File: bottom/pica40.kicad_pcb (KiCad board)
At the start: 2 copper layers, 135 x 93.7 mm, 5 parts

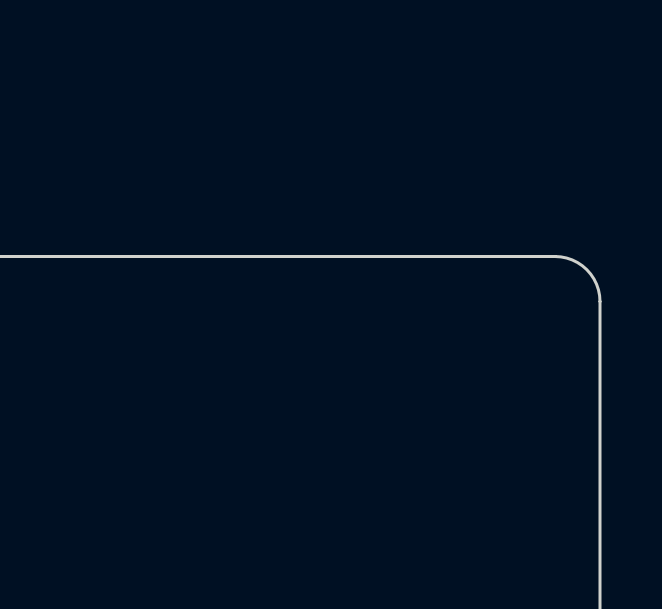
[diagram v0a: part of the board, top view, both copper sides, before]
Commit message: logos and jlcpcb texts
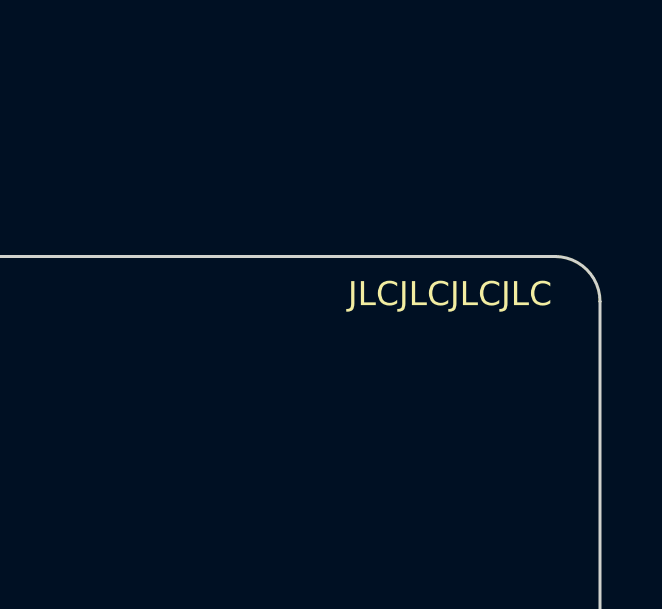
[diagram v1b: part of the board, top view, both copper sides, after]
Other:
- board text added: "JLCJLCJLCJLC"
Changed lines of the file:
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@@
   (gr_line (start 68.5 76) (end 68.5 111) (layer "Edge.Cuts") (width 0.1))
   (gr_line (start 154 132.5) (end 172.5 137.5) (layer "Edge.Cuts") (width 0.1))
+  (gr_text "JLCJLCJLCJLC" (at 198.5 59.25) (layer "F.SilkS")
+    (effects (font (size 0.8 0.8) (thickness 0.15)))
+  )
 )
